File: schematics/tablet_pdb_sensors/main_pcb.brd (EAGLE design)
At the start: 100 x 80 mm, 10 parts

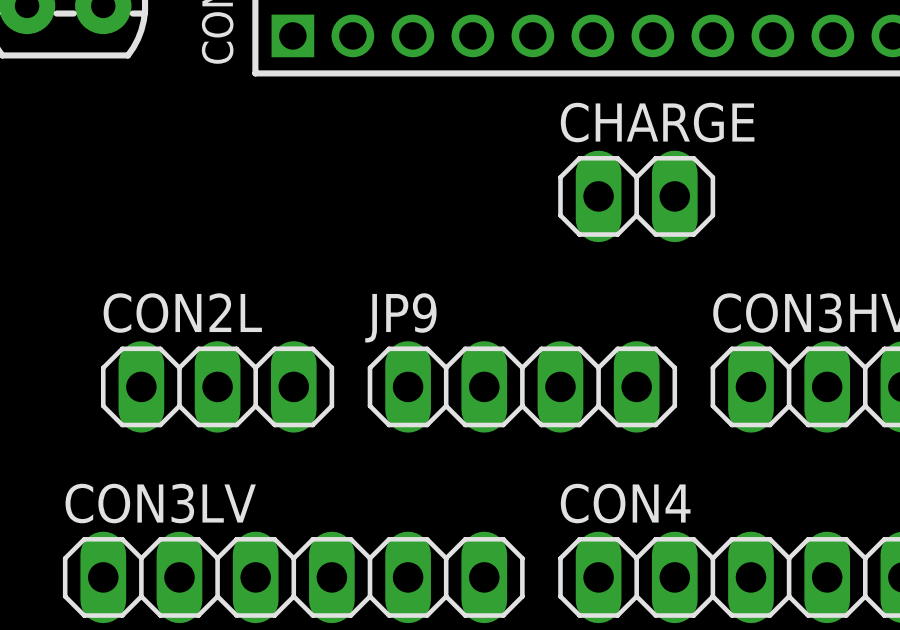
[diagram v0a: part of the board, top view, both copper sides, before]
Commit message: Wired up fuel cell and charger
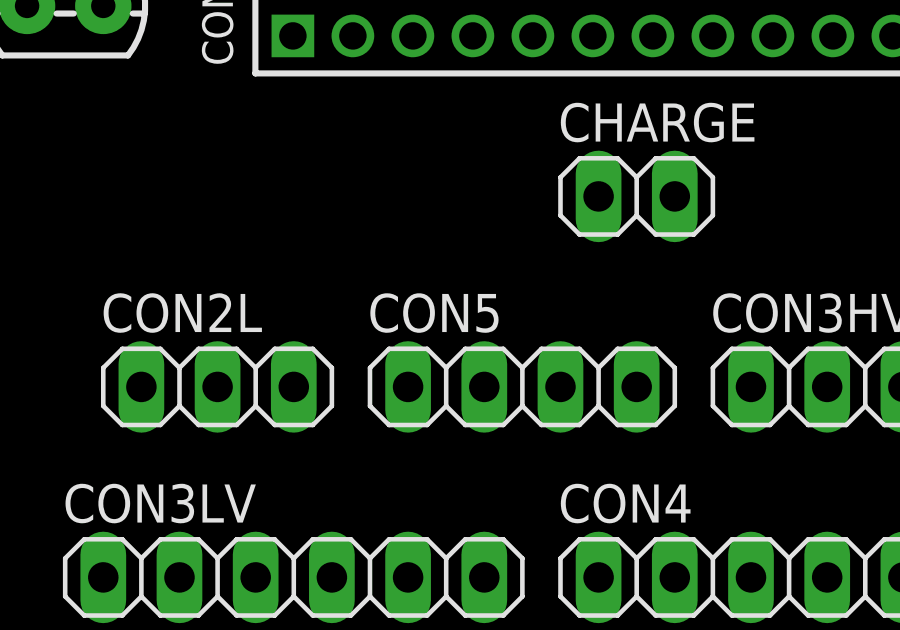
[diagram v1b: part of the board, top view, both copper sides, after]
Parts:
- renumbered JP9 to CON5
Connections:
- removed net CON2_SDA: CON2R.1
- removed net CON2_SDL: CON2R.2
- removed net CON4_SCL: CON3HV.2, CON4.1
- removed net CON4_SDA: CON3HV.3, CON4.2
- new net A4: CON3LV.5
- new net EN: CON5.4
- new net HV_I2C.SDA: CON2R.1, CON3HV.3, CON4.2
- new net HV_I2C.SDL: CON2R.2, CON3HV.2, CON4.1
- new net LV_DRDY: CON3LV.4
- new net PS: CON5.1
- net HV_GND: now also CON5.3
- net HV_VCC: now also CON5.2
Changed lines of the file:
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@@
 <element name="CON4" library="pinhead" package="1X08" value="" x="-24.13" y="11.43"/>
 <element name="CHARGE" library="pinhead" package="1X02" value="" x="-31.75" y="24.13"/>
-<element name="JP9" library="pinhead" package="1X04" value="" x="-35.56" y="17.78"/>
+<element name="CON5" library="pinhead" package="1X04" value="" x="-35.56" y="17.78"/>
 <element name="Q1" library="SparkFun-DiscreteSemi" package="TO-92" value="" x="-50.8" y="30.48">
 <attribute name="PROD_ID" value="TRANS-08447" x="-50.8" y="30.48" size="1.778" layer="27" display="off"/>
@@
 <contactref element="CON2L" pad="3"/>
 </signal>
-<signal name="CON2_SDA">
+<signal name="HV_I2C.SDA">
 <contactref element="CON2R" pad="1"/>
-</signal>
-<signal name="CON2_SDL">
-<contactref element="CON2R" pad="2"/>
+<contactref element="CON4" pad="2"/>
+<contactref element="CON3HV" pad="3"/>
+<wire x1="-22.86" y1="17.78" x2="-30.48" y2="11.43" width="0" layer="19" extent="1-1"/>
+<wire x1="-20.32" y1="24.13" x2="-22.86" y2="17.78" width="0" layer="19" extent="1-1"/>
 </signal>
 <signal name="CON2_QST">
@@
 <wire x1="-15.21" y1="31.48" x2="-36.83" y2="11.43" width="0" layer="19" extent="1-1"/>
 </signal>
-<signal name="HV_VCC">
-<contactref element="CON3HV" pad="1"/>
-<contactref element="CON4" pad="7"/>
-<wire x1="-17.78" y1="11.43" x2="-27.94" y2="17.78" width="0" layer="19" extent="1-1"/>
-</signal>
 <signal name="B4">
 <contactref element="CON3HV" pad="5"/>
@@
 <contactref element="CON3HV" pad="6"/>
 <contactref element="CON4" pad="6"/>
+<contactref element="CON5" pad="3"/>
+<wire x1="-20.32" y1="11.43" x2="-34.29" y2="17.78" width="0" layer="19" extent="1-1"/>
 <wire x1="-15.24" y1="17.78" x2="-20.32" y2="11.43" width="0" layer="19" extent="1-1"/>
 </signal>
@@
 </signal>
 <signal name="LV_I2C.SCL">
+<contactref element="CON3LV" pad="2"/>
 <contactref element="CON1" pad="14"/>
-<contactref element="CON3LV" pad="2"/>
 <wire x1="-31.21" y1="31.48" x2="-46.99" y2="11.43" width="0" layer="19" extent="1-1"/>
 </signal>
 <signal name="LV_I2C.SDA">
+<contactref element="CON3LV" pad="3"/>
 <contactref element="CON1" pad="16"/>
-<contactref element="CON3LV" pad="3"/>
 <wire x1="-29.21" y1="31.48" x2="-44.45" y2="11.43" width="0" layer="19" extent="1-1"/>
 </signal>
-<signal name="CON4_SCL">
+<signal name="PS">
+<contactref element="CON5" pad="1"/>
+</signal>
+<signal name="EN">
+<contactref element="CON5" pad="4"/>
+</signal>
+<signal name="HV_VCC">
+<contactref element="CON3HV" pad="1"/>
+<contactref element="CON4" pad="7"/>
+<contactref element="CON5" pad="2"/>
+<wire x1="-27.94" y1="17.78" x2="-36.83" y2="17.78" width="0" layer="19" extent="1-1"/>
+<wire x1="-17.78" y1="11.43" x2="-27.94" y2="17.78" width="0" layer="19" extent="1-1"/>
+</signal>
+<signal name="A4">
+<contactref element="CON3LV" pad="5"/>
+</signal>
+<signal name="LV_DRDY">
+<contactref element="CON3LV" pad="4"/>
+</signal>
+<signal name="HV_I2C.SDL">
+<contactref element="CON3HV" pad="2"/>
 <contactref element="CON4" pad="1"/>
-<contactref element="CON3HV" pad="2"/>
+<contactref element="CON2R" pad="2"/>
 <wire x1="-25.4" y1="17.78" x2="-33.02" y2="11.43" width="0" layer="19" extent="1-1"/>
-</signal>
-<signal name="CON4_SDA">
-<contactref element="CON4" pad="2"/>
-<contactref element="CON3HV" pad="3"/>
-<wire x1="-22.86" y1="17.78" x2="-30.48" y2="11.43" width="0" layer="19" extent="1-1"/>
+<wire x1="-17.78" y1="24.13" x2="-25.4" y2="17.78" width="0" layer="19" extent="1-1"/>
 </signal>
 </signals>

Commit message: Completed schematic
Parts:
- removed CHARGE: (no value), pinhead:1X02
- removed CON5: (no value), pinhead:1X04
- removed Q1: (no value), SparkFun-DiscreteSemi:TO-92
- added CON5L, CON6, CON7LED, CON7SWITCH, CON8: (no value), pinhead:1X02
- added CON5R: (no value), pinhead:1X04
- added H1, H2, H3, H4: MOUNT-HOLE2.8, holes:2,8
- added LOGO1: OSHW-LOGOL, SparkFun-Aesthetics:OSHW-LOGO-L
- added R.LED, R.PULLUP: (no value), resistor:0204V
- CON1: device pinhead-2:2X15M -> pinhead:2X20
- moved CON3LV 89.3 mm to (43.2, 34.3), turned to 90 degrees
- moved CON4 74.1 mm to (39.4, 49.5)
- moved CON1 58.6 mm to (26.7, 12.7)
- moved CON3HV 57.1 mm to (33.0, 34.3), turned to 90 degrees
- moved CON2L 50.6 mm to (3.81, 27.9), turned to 270 degrees
- moved CON2R 29.5 mm to (11.4, 27.9), turned to 270 degrees
- moved FRAME1 9.16 mm to (-96.5, -6.35)
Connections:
- new net N$1: CON7LED.1, R.LED.2
- new net SIG.LED1: CON1.16, R.LED.1
- new net SIG.LED2: CON1.18, CON7LED.2
- new net SIG.SWITCH: CON1.15, CON7SWITCH.1, R.PULLUP.1
- net EN: now also CON5R.4; no longer CON5.4
- net GND: now also CON5L.2, CON6.2; no longer CHARGE.2
- net HV_GND: now also CON5R.3, CON8.2; no longer CON5.3
- net HV_VCC: now also CON5R.2, CON8.1; no longer CON5.2
- net LV_GND: now also CON1.25, CON7SWITCH.2; no longer CON1.30
- net LV_I2C.SCL: now also CON1.5; no longer CON1.14
- net LV_I2C.SDA: now also CON1.3; no longer CON1.16
- net LV_VCC: now also CON1.1, R.PULLUP.2; no longer CON1.29
- net PS: now also CON5R.1; no longer CON5.1
- net VIN: now also CON5L.1, CON6.1; no longer CHARGE.1
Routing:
- net LV_GND: track 0.00 -> 129.5 mm
- net HV_I2C.SDL: track 0.00 -> 117.9 mm
- net LV_I2C.SDA: track 0.00 -> 97.8 mm, vias 0 -> 1
- net HV_VCC: track 0.00 -> 97.1 mm, vias 0 -> 1
- net LV_I2C.SCL: track 0.00 -> 92.7 mm, vias 0 -> 2
- net LV_VCC: track 0.00 -> 89.7 mm, vias 0 -> 1
- net SIG.SWITCH: track 0.00 -> 88.9 mm, vias 0 -> 1
- net HV_GND: track 0.00 -> 84.0 mm, vias 0 -> 1
- net HV_I2C.SDA: track 0.00 -> 42.7 mm
- net DRDY: track 0.00 -> 21.6 mm
- net SIG.LED2: track 0.00 -> 11.4 mm
- net SIG.LED1: track 0.00 -> 8.15 mm
- net N$1: track 0.00 -> 7.62 mm
- net VIN: track 0.00 -> 6.35 mm
- net GND: track 0.00 -> 6.35 mm
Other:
- board size 100 x 80 mm -> 66 x 91.4 mm
- board text added: "Designed by Joseph D"
- board text added: "Ensure magic smoke level is sufficient for successful operation"
- board text added: "outurnate.com"
